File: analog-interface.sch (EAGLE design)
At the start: 18 parts, among them U1 ISL3179EIBZ, U2 ATMEGA328P

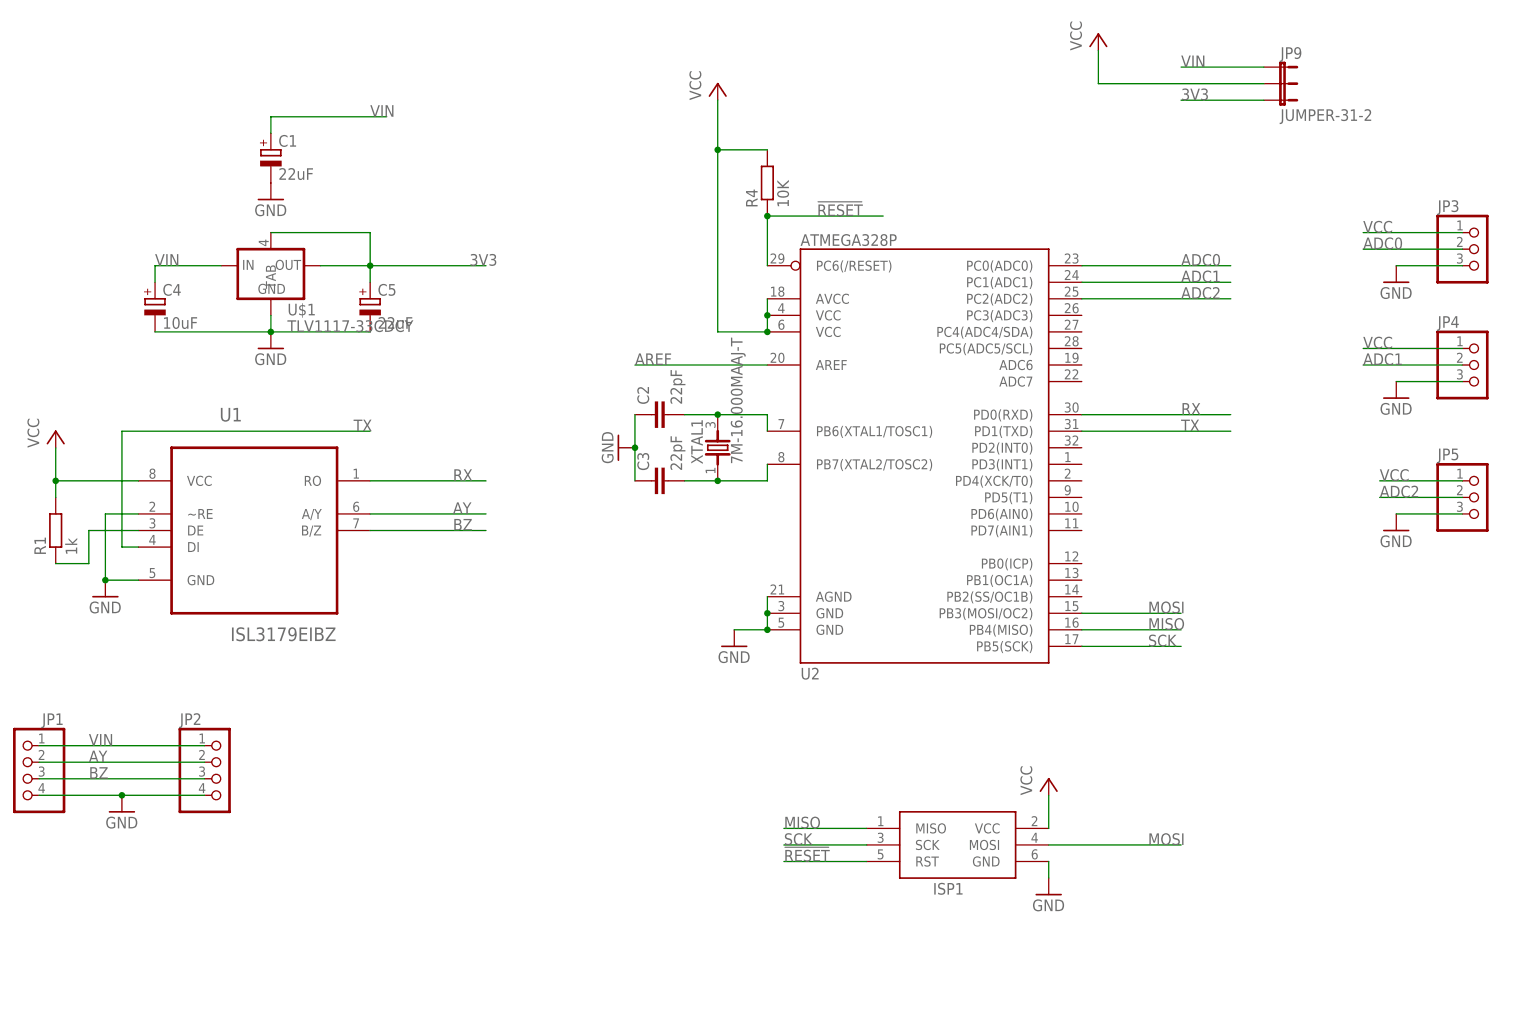
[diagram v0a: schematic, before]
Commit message: done a lot of routing added vref chip
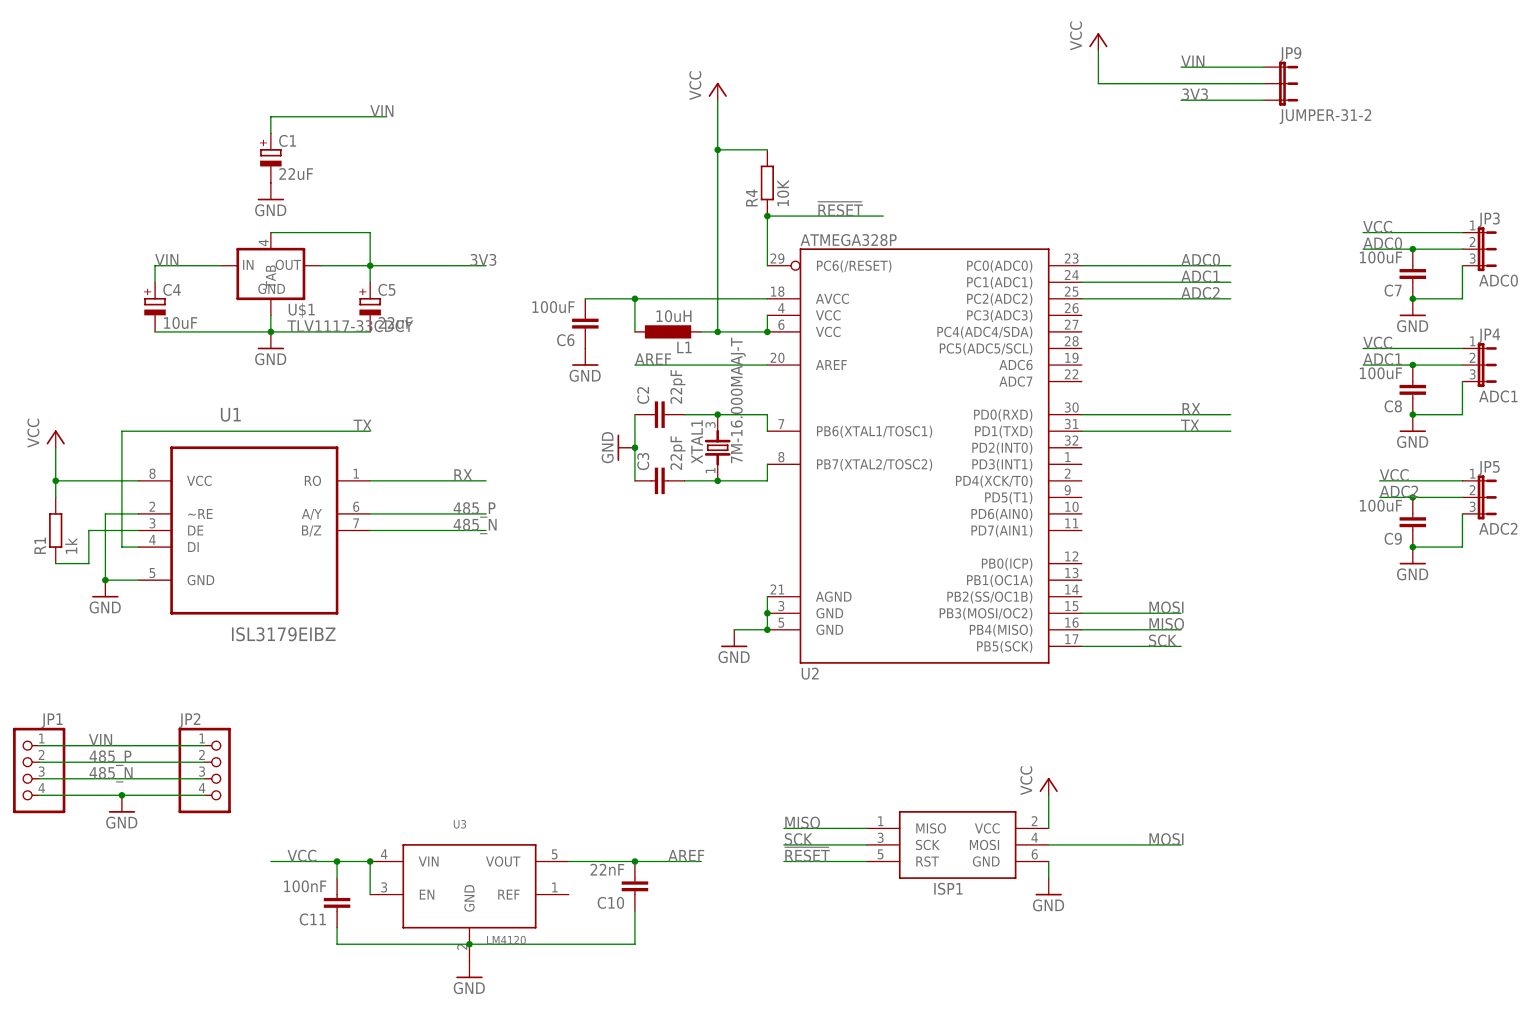
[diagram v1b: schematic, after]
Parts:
- added C10: 22nF, resistor:C-EUC0805
- added C11: 100nF, resistor:C-EUC0805
- added C6, C7, C8, C9: 100uF, resistor:C-EUC0805
- added L1: 10uH, resistor:L-EUL3216C
- added U3: LM4120, mountainsensing:LM4120
- JP3: value (none) -> ADC0; device pinhead:PINHD-1X3 -> farnell-parts:3-PIN-MOLEX
- JP4: value (none) -> ADC1; device pinhead:PINHD-1X3 -> farnell-parts:3-PIN-MOLEX
- JP5: value (none) -> ADC2; device pinhead:PINHD-1X3 -> farnell-parts:3-PIN-MOLEX
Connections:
- net AY renamed 485_P
- net BZ renamed 485_N
- new net N$4: C6.2, L1.1, U2.AVCC
- new net N$7: C10.1, C11.1
- net ADC0: now also C7.2
- net ADC1: now also C8.2
- net ADC2: now also C9.2
- net AREF: now also C10.2, U3.VOUT
- net GND: now also C6.1, C7.1, C8.1, C9.1, U3.GND
- net VCC: now also C11.2, L1.2, U3.EN, U3.VIN; no longer U2.AVCC
